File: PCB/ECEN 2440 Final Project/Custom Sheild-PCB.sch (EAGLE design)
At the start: 7 parts, among them J8 SD_CARD_SOCKET

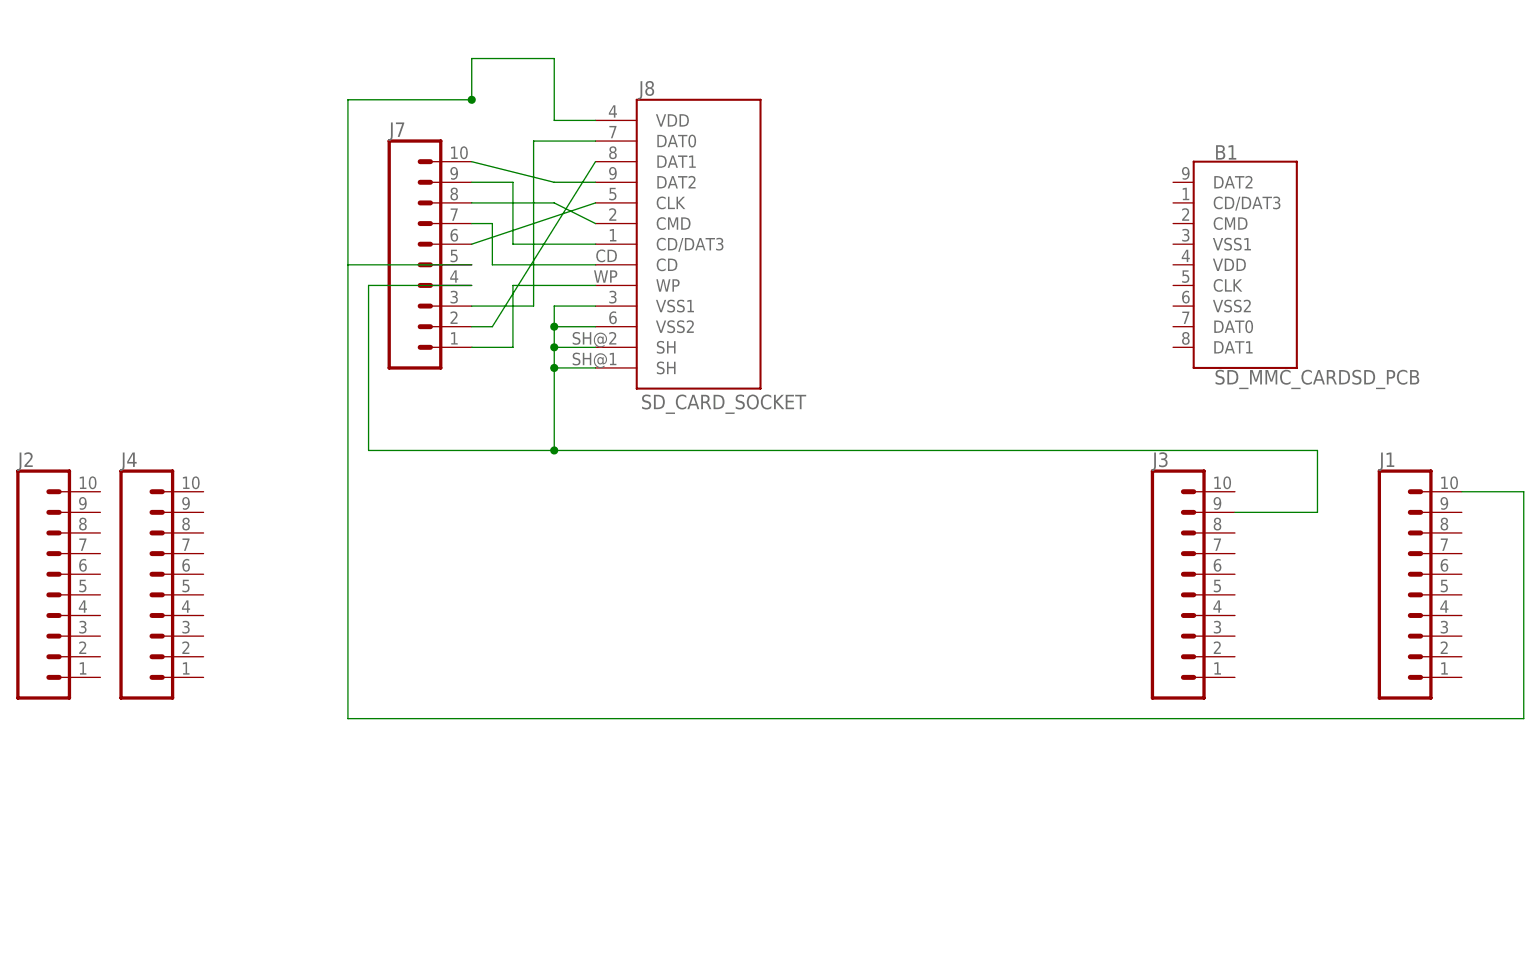
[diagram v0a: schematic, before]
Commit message: Created library and made altimeter
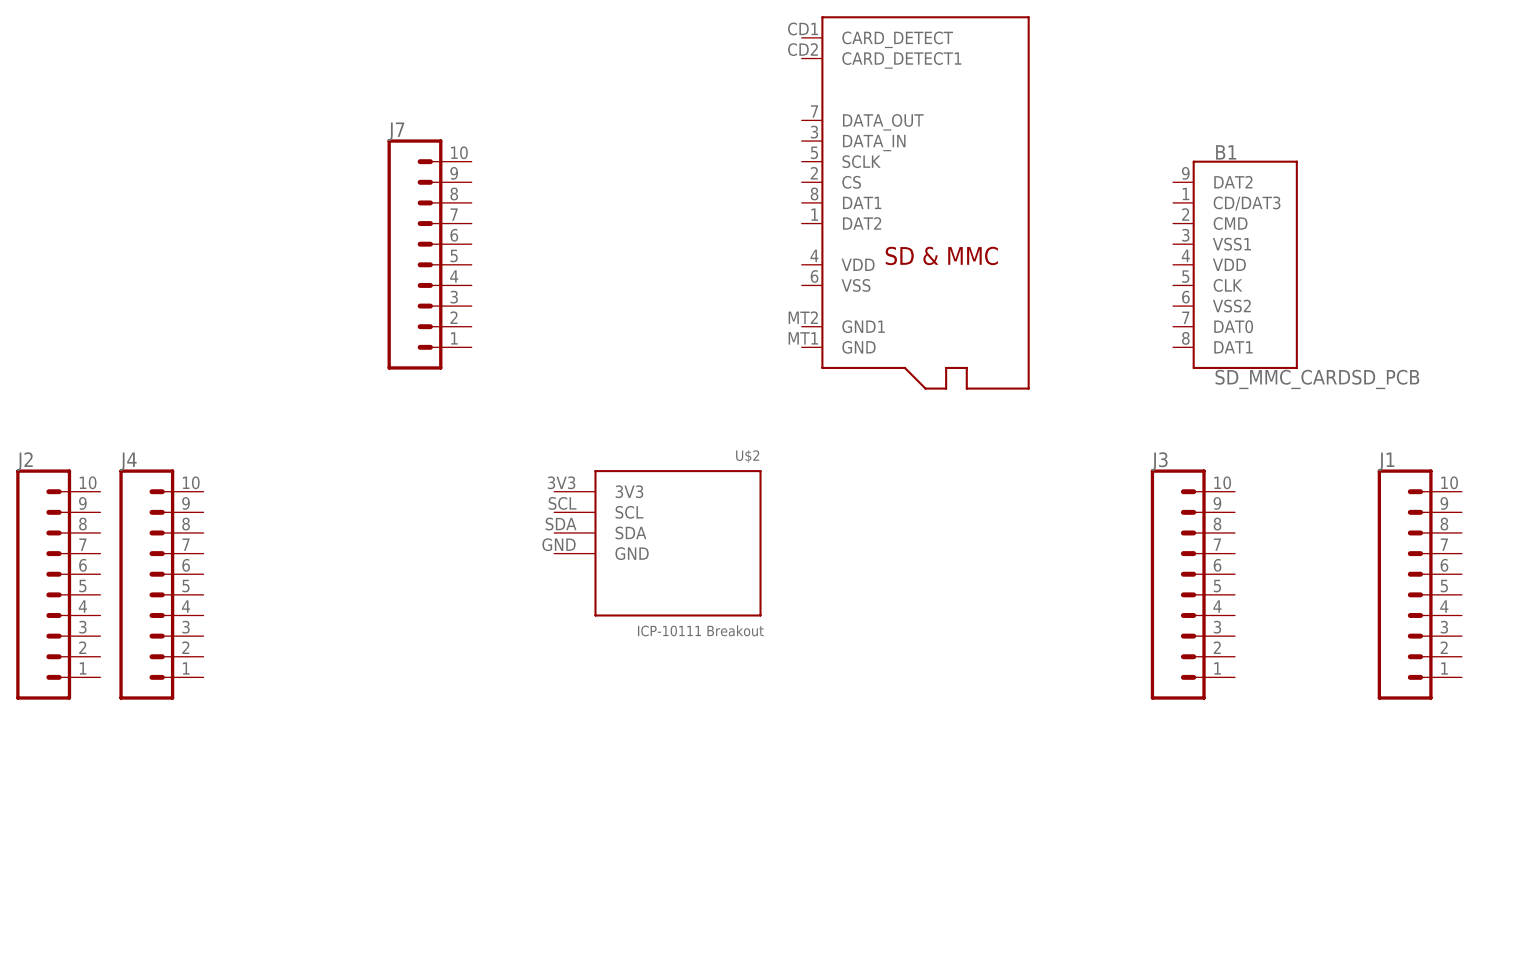
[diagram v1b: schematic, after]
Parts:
- removed J8: SD_CARD_SOCKET, SparkFun-Connectors:SD_CARD_SOCKET
- added U$1: MICROSD, adafruit:MICROSD
- added U$2: ALTIMETER, Custom Library:ALTIMETER
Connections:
- removed net N$10: J1.10, J7.5, J8.VDD
- removed net N$11: J3.9, J7.4, J8.SH@1, J8.SH@2, J8.VSS1, J8.VSS2
- removed net N$2: J7.1, J8.WP
- removed net N$3: J7.7, J8.CD
- removed net N$4: J7.9, J8.CD/DAT3
- removed net N$5: J7.8, J8.CMD
- removed net N$6: J7.6, J8.CLK
- removed net N$7: J7.10, J8.DAT2
- removed net N$8: J7.2, J8.DAT1
- removed net N$9: J7.3, J8.DAT0
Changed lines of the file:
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@@
 <part name="J4" library="SparkFun-Connectors" library_urn="urn:adsk.eagle:library:513" deviceset="CONN_10" device="&quot;" package3d_urn="urn:adsk.eagle:package:38157/1"/>
 <part name="J7" library="SparkFun-Connectors" library_urn="urn:adsk.eagle:library:513" deviceset="CONN_10" device="&quot;" package3d_urn="urn:adsk.eagle:package:38157/1"/>
-<part name="J8" library="SparkFun-Connectors" library_urn="urn:adsk.eagle:library:513" deviceset="SD_CARD_SOCKET" device="" package3d_urn="urn:adsk.eagle:package:38262/1"/>
 <part name="B1" library="SparkFun-Boards" library_urn="urn:adsk.eagle:library:509" deviceset="SD_MMC_CARD" device="SD_PCB" package3d_urn="urn:adsk.eagle:package:37313/1"/>
+<part name="U$1" library="adafruit" library_urn="urn:adsk.eagle:library:420" deviceset="MICROSD" device="" package3d_urn="urn:adsk.eagle:package:6240723/1"/>
+<part name="U$2" library="Custom Library" deviceset="ALTIMETER" device=""/>
 </parts>
 <sheets>
@@
 <attribute name="NAME" x="30.48" y="99.568" size="1.778" layer="95" font="vector"/>
 </instance>
-<instance part="J8" gate="G$1" x="68.58" y="86.36" smashed="yes">
-<attribute name="NAME" x="61.214" y="104.648" size="1.778" layer="95" font="vector"/>
-<attribute name="VALUE" x="61.468" y="66.04" size="1.778" layer="96" font="vector"/>
-</instance>
 <instance part="B1" gate="G$1" x="137.16" y="83.82" smashed="yes">
 <attribute name="NAME" x="132.08" y="96.774" size="1.778" layer="95" font="vector"/>
 <attribute name="VALUE" x="132.08" y="70.866" size="1.778" layer="96" font="vector" align="top-left"/>
+</instance>
+<instance part="U$1" gate="G$1" x="99.06" y="93.98" smashed="yes"/>
+<instance part="U$2" gate="G$1" x="55.88" y="40.64" smashed="yes">
+<attribute name="NAME" x="76.2" y="60.96" size="1.27" layer="95" rot="R180"/>
 </instance>
 </instances>
@@
 </busses>
 <nets>
-<net name="N$2" class="0">
-<segment>
-<pinref part="J8" gate="G$1" pin="WP"/>
-<wire x1="55.88" y1="81.28" x2="45.72" y2="81.28" width="0.1524" layer="91"/>
-<wire x1="45.72" y1="81.28" x2="45.72" y2="73.66" width="0.1524" layer="91"/>
-<pinref part="J7" gate="G$1" pin="1"/>
-<wire x1="45.72" y1="73.66" x2="40.64" y2="73.66" width="0.1524" layer="91"/>
-</segment>
-</net>
-<net name="N$3" class="0">
-<segment>
-<pinref part="J8" gate="G$1" pin="CD"/>
-<wire x1="55.88" y1="83.82" x2="43.18" y2="83.82" width="0.1524" layer="91"/>
-<wire x1="43.18" y1="83.82" x2="43.18" y2="88.9" width="0.1524" layer="91"/>
-<pinref part="J7" gate="G$1" pin="7"/>
-<wire x1="43.18" y1="88.9" x2="40.64" y2="88.9" width="0.1524" layer="91"/>
-</segment>
-</net>
-<net name="N$4" class="0">
-<segment>
-<wire x1="45.72" y1="86.36" x2="45.72" y2="93.98" width="0.1524" layer="91"/>
-<pinref part="J7" gate="G$1" pin="9"/>
-<wire x1="45.72" y1="93.98" x2="40.64" y2="93.98" width="0.1524" layer="91"/>
-<pinref part="J8" gate="G$1" pin="CD/DAT3"/>
-<wire x1="45.72" y1="86.36" x2="55.88" y2="86.36" width="0.1524" layer="91"/>
-</segment>
-</net>
-<net name="N$5" class="0">
-<segment>
-<pinref part="J8" gate="G$1" pin="CMD"/>
-<wire x1="55.88" y1="88.9" x2="50.8" y2="91.44" width="0.1524" layer="91"/>
-<pinref part="J7" gate="G$1" pin="8"/>
-<wire x1="50.8" y1="91.44" x2="40.64" y2="91.44" width="0.1524" layer="91"/>
-</segment>
-</net>
-<net name="N$6" class="0">
-<segment>
-<pinref part="J8" gate="G$1" pin="CLK"/>
-<pinref part="J7" gate="G$1" pin="6"/>
-<wire x1="55.88" y1="91.44" x2="40.64" y2="86.36" width="0.1524" layer="91"/>
-</segment>
-</net>
-<net name="N$7" class="0">
-<segment>
-<pinref part="J8" gate="G$1" pin="DAT2"/>
-<pinref part="J7" gate="G$1" pin="10"/>
-<wire x1="55.88" y1="93.98" x2="50.8" y2="93.98" width="0.1524" layer="91"/>
-<wire x1="50.8" y1="93.98" x2="40.64" y2="96.52" width="0.1524" layer="91"/>
-</segment>
-</net>
-<net name="N$8" class="0">
-<segment>
-<pinref part="J8" gate="G$1" pin="DAT1"/>
-<wire x1="55.88" y1="96.52" x2="43.18" y2="76.2" width="0.1524" layer="91"/>
-<pinref part="J7" gate="G$1" pin="2"/>
-<wire x1="43.18" y1="76.2" x2="40.64" y2="76.2" width="0.1524" layer="91"/>
-</segment>
-</net>
-<net name="N$9" class="0">
-<segment>
-<pinref part="J8" gate="G$1" pin="DAT0"/>
-<wire x1="55.88" y1="99.06" x2="48.26" y2="99.06" width="0.1524" layer="91"/>
-<wire x1="48.26" y1="99.06" x2="48.26" y2="78.74" width="0.1524" layer="91"/>
-<pinref part="J7" gate="G$1" pin="3"/>
-<wire x1="48.26" y1="78.74" x2="40.64" y2="78.74" width="0.1524" layer="91"/>
-</segment>
-</net>
-<net name="N$10" class="0">
-<segment>
-<pinref part="J8" gate="G$1" pin="VDD"/>
-<wire x1="55.88" y1="101.6" x2="50.8" y2="101.6" width="0.1524" layer="91"/>
-<wire x1="50.8" y1="101.6" x2="50.8" y2="109.22" width="0.1524" layer="91"/>
-<pinref part="J7" gate="G$1" pin="5"/>
-<wire x1="40.64" y1="83.82" x2="25.4" y2="83.82" width="0.1524" layer="91"/>
-<wire x1="25.4" y1="83.82" x2="25.4" y2="104.14" width="0.1524" layer="91"/>
-<wire x1="40.64" y1="104.14" x2="25.4" y2="104.14" width="0.1524" layer="91"/>
-<wire x1="25.4" y1="83.82" x2="25.4" y2="27.94" width="0.1524" layer="91"/>
-<wire x1="25.4" y1="27.94" x2="170.18" y2="27.94" width="0.1524" layer="91"/>
-<pinref part="J1" gate="G$1" pin="10"/>
-<wire x1="170.18" y1="27.94" x2="170.18" y2="55.88" width="0.1524" layer="91"/>
-<wire x1="170.18" y1="55.88" x2="162.56" y2="55.88" width="0.1524" layer="91"/>
-<wire x1="50.8" y1="109.22" x2="40.64" y2="109.22" width="0.1524" layer="91"/>
-<wire x1="40.64" y1="109.22" x2="40.64" y2="104.14" width="0.1524" layer="91"/>
-<junction x="40.64" y="104.14"/>
-</segment>
-</net>
-<net name="N$11" class="0">
-<segment>
-<pinref part="J7" gate="G$1" pin="4"/>
-<wire x1="40.64" y1="81.28" x2="27.94" y2="81.28" width="0.1524" layer="91"/>
-<pinref part="J8" gate="G$1" pin="VSS1"/>
-<wire x1="55.88" y1="78.74" x2="50.8" y2="78.74" width="0.1524" layer="91"/>
-<wire x1="50.8" y1="78.74" x2="50.8" y2="76.2" width="0.1524" layer="91"/>
-<pinref part="J8" gate="G$1" pin="VSS2"/>
-<wire x1="50.8" y1="71.12" x2="50.8" y2="73.66" width="0.1524" layer="91"/>
-<wire x1="50.8" y1="73.66" x2="50.8" y2="76.2" width="0.1524" layer="91"/>
-<wire x1="50.8" y1="76.2" x2="55.88" y2="76.2" width="0.1524" layer="91"/>
-<pinref part="J8" gate="G$1" pin="SH@2"/>
-<wire x1="50.8" y1="73.66" x2="55.88" y2="73.66" width="0.1524" layer="91"/>
-<pinref part="J8" gate="G$1" pin="SH@1"/>
-<wire x1="50.8" y1="71.12" x2="55.88" y2="71.12" width="0.1524" layer="91"/>
-<wire x1="50.8" y1="71.12" x2="50.8" y2="60.96" width="0.1524" layer="91"/>
-<wire x1="50.8" y1="60.96" x2="144.78" y2="60.96" width="0.1524" layer="91"/>
-<pinref part="J3" gate="G$1" pin="9"/>
-<wire x1="144.78" y1="60.96" x2="144.78" y2="53.34" width="0.1524" layer="91"/>
-<wire x1="144.78" y1="53.34" x2="134.62" y2="53.34" width="0.1524" layer="91"/>
-<junction x="50.8" y="76.2"/>
-<junction x="50.8" y="73.66"/>
-<junction x="50.8" y="71.12"/>
-<wire x1="27.94" y1="81.28" x2="27.94" y2="60.96" width="0.1524" layer="91"/>
-<wire x1="27.94" y1="60.96" x2="50.8" y2="60.96" width="0.1524" layer="91"/>
-<junction x="50.8" y="60.96"/>
-</segment>
-</net>
 </nets>
 </sheet>

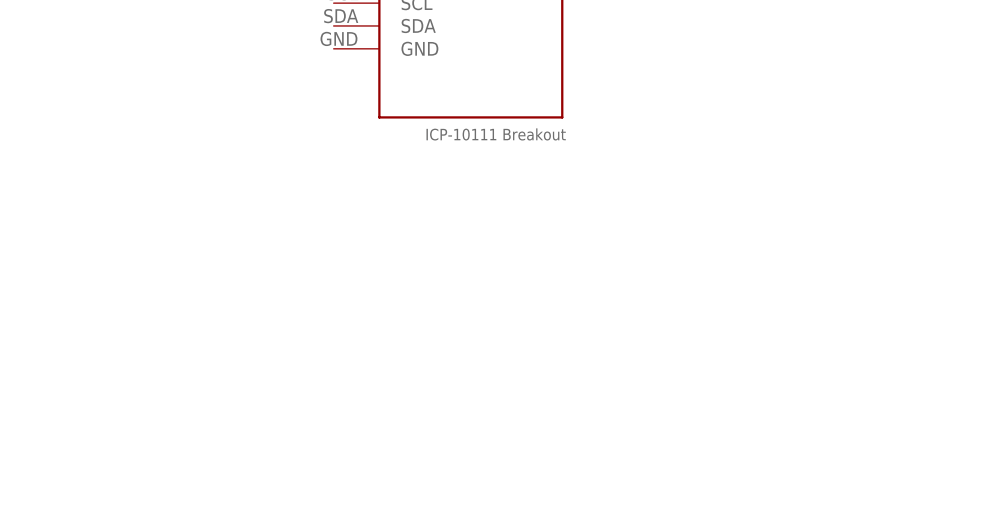
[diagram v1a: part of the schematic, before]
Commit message: Made MSP432 and fixed other components
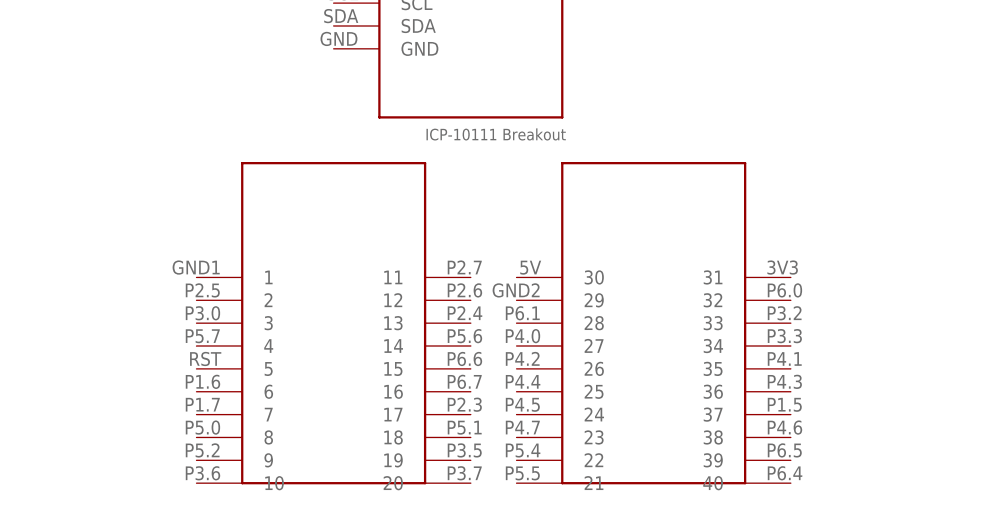
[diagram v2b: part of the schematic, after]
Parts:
- added U$3: MSP432, Custom Library:MSP432
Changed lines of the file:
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@@
 <layer number="115" name="ReferenceISLANDS" color="7" fill="1" visible="yes" active="yes"/>
 <layer number="116" name="Patch_BOT" color="9" fill="4" visible="yes" active="yes"/>
+<layer number="117" name="BACKMAAT1" color="7" fill="1" visible="no" active="no"/>
 <layer number="118" name="Rect_Pads" color="7" fill="1" visible="yes" active="yes"/>
+<layer number="119" name="KAP_TEKEN" color="7" fill="1" visible="no" active="no"/>
+<layer number="120" name="KAP_MAAT1" color="7" fill="1" visible="no" active="no"/>
 <layer number="121" name="_tsilk" color="7" fill="1" visible="yes" active="yes"/>
 <layer number="122" name="_bsilk" color="7" fill="1" visible="yes" active="yes"/>
@@
 <layer number="128" name="_bValues" color="7" fill="1" visible="yes" active="yes"/>
 <layer number="129" name="Mask" color="7" fill="1" visible="yes" active="yes"/>
+<layer number="130" name="130bmp" color="2" fill="1" visible="no" active="yes"/>
 <layer number="131" name="tAdjust" color="7" fill="1" visible="yes" active="yes"/>
 <layer number="132" name="bAdjust" color="7" fill="1" visible="yes" active="yes"/>
 <layer number="144" name="Drill_legend" color="7" fill="1" visible="yes" active="yes"/>
+<layer number="145" name="DrillLegend_01-16" color="2" fill="9" visible="no" active="yes"/>
 <layer number="150" name="Notes" color="7" fill="1" visible="yes" active="yes"/>
 <layer number="151" name="HeatSink" color="7" fill="1" visible="yes" active="yes"/>
@@
 <part name="U$1" library="adafruit" library_urn="urn:adsk.eagle:library:420" deviceset="MICROSD" device="" package3d_urn="urn:adsk.eagle:package:6240723/1"/>
 <part name="U$2" library="Custom Library" deviceset="ALTIMETER" device=""/>
+<part name="U$3" library="Custom Library" deviceset="MSP432" device=""/>
 </parts>
 <sheets>
@@
 <attribute name="NAME" x="76.2" y="60.96" size="1.27" layer="95" rot="R180"/>
 </instance>
+<instance part="U$3" gate="MSP432" x="50.8" y="27.94" smashed="yes"/>
 </instances>
 <busses>
